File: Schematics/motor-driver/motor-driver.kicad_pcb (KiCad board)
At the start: 2 copper layers, 99.1 x 74.9 mm, 17 parts, among them J1 Conn_01x02_Male, U1 encoder-motor, U2 encoder-motor, U3 encoder-motor, U4 encoder-motor, U5 TB6612-breakout, U6 TB6612-breakout, U7 Teensy3.2

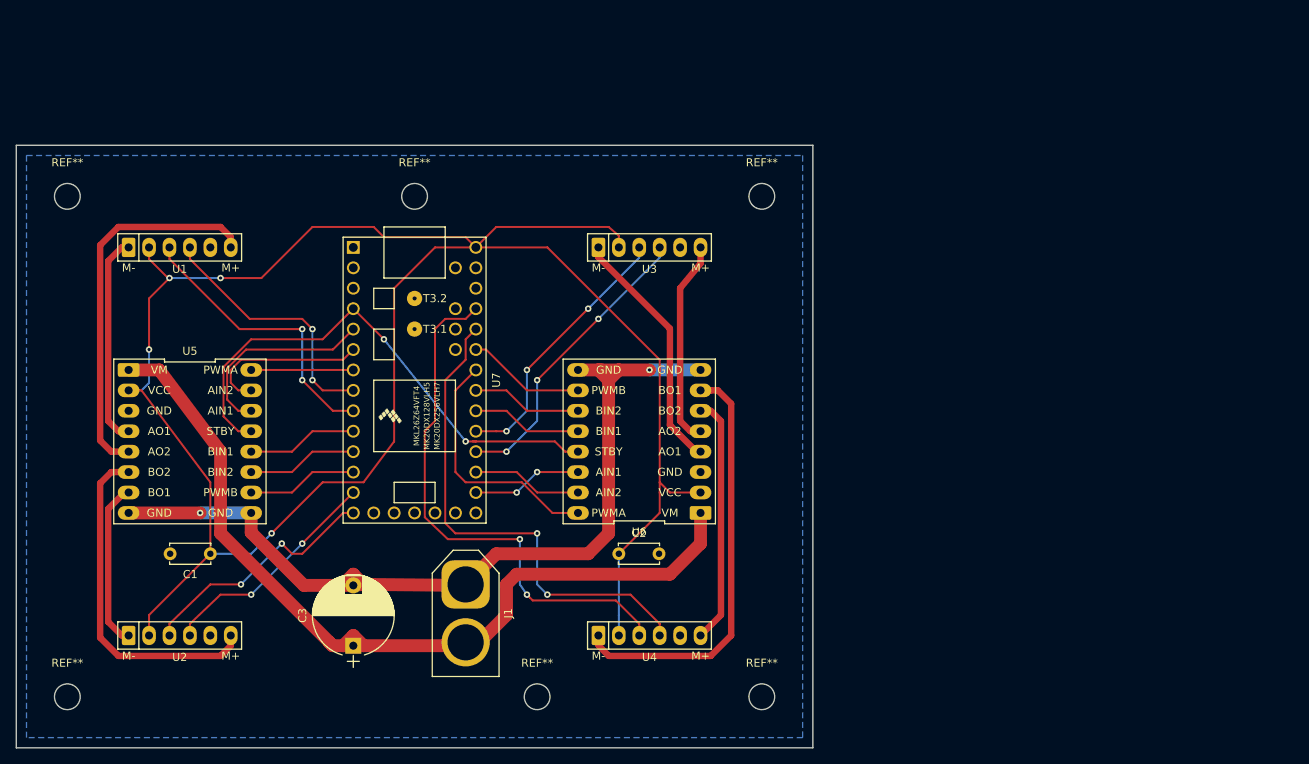
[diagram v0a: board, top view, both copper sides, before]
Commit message: Add mounting holes to PCB
Update submodule remote
Remove files that should just be wiki pages

#28, #16
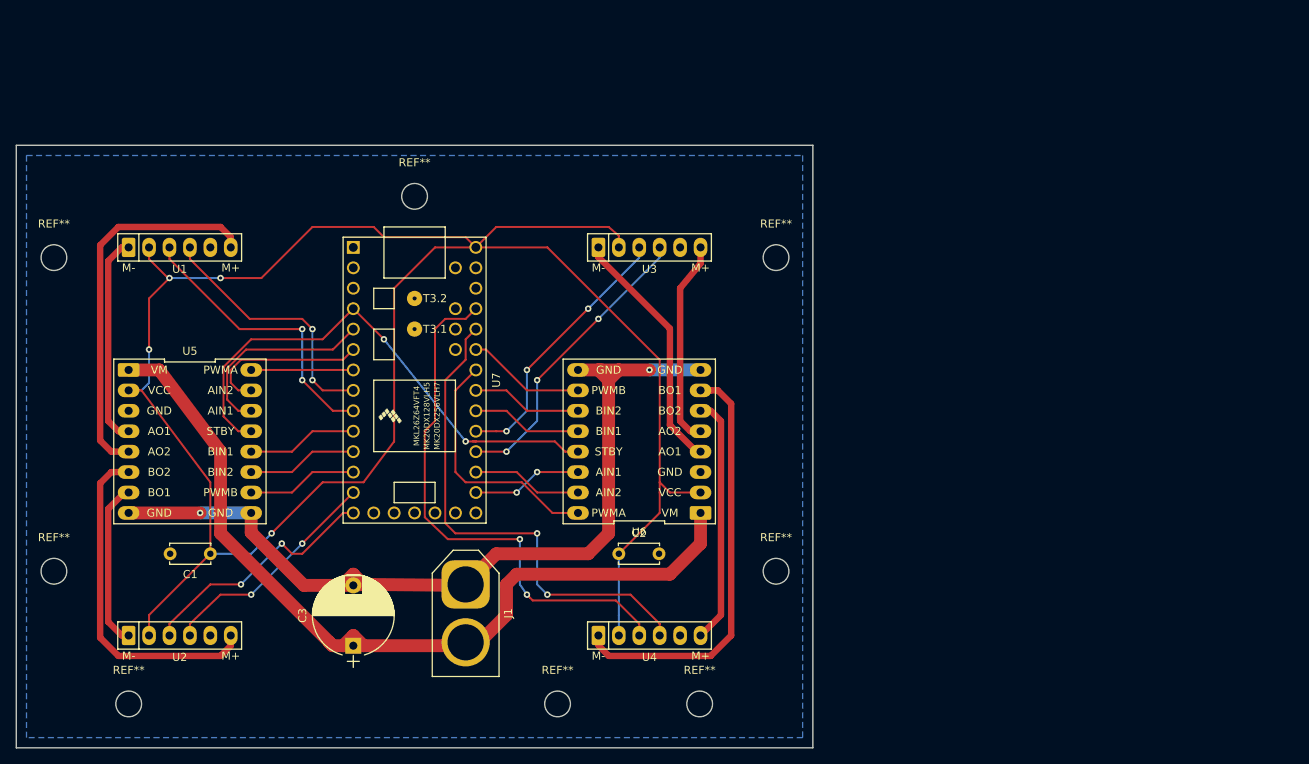
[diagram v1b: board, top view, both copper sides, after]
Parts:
- removed the REF** at (132.1, 105.4)
- removed the REF** at (45.7, 105.4)
- added REF**: MountingHole_3.2mm_M3, Mounting_Holes:MountingHole_3.2mm_M3, F.Cu at (106.7, 106.3)
- added REF**: MountingHole_3.2mm_M3, Mounting_Holes:MountingHole_3.2mm_M3, F.Cu at (53.4, 106.3)
- added REF**: MountingHole_3.2mm_M3, Mounting_Holes:MountingHole_3.2mm_M3, F.Cu at (133.8, 89.8)
- added REF**: MountingHole_3.2mm_M3, Mounting_Holes:MountingHole_3.2mm_M3, F.Cu at (44.0, 89.8)
- moved REF** 88.5 mm to (133.8, 50.8)
- moved REF** 88.4 mm to (44.0, 50.8)
- moved REF** 20.2 mm to (124.3, 106.3)
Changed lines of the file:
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@@
     (tracks 284)
     (zones 0)
-    (modules 17)
+    (modules 19)
     (nets 48)
   )
@@
       (drillshape 0)
       (scaleselection 1)
-      (outputdirectory ""))
+      (outputdirectory "plot/"))
   )
   (net 0 "")
@@
   )
   (module Mounting_Holes:MountingHole_3.2mm_M3 (layer F.Cu)
+    (at 106.68 106.3)
+    (descr "Mounting Hole 3.2mm, no annular, M3")
+    (tags "mounting hole 3.2mm no annular m3")
+    (attr virtual)
+    (fp_text reference REF** (at 0 -4.2) (layer F.SilkS)
+      (effects (font (size 1 1) (thickness 0.15)))
+    )
+    (fp_text value MountingHole_3.2mm_M3 (at 0 4.2) (layer F.Fab)
+      (effects (font (size 1 1) (thickness 0.15)))
+    )
+    (fp_circle (center 0 0) (end 3.45 0) (layer F.CrtYd) (width 0.05))
+    (fp_circle (center 0 0) (end 3.2 0) (layer Cmts.User) (width 0.15))
+    (fp_text user %R (at 0.3 0) (layer F.Fab)
+      (effects (font (size 1 1) (thickness 0.15)))
+    )
+    (pad 1 np_thru_hole circle (at 0 0) (size 3.2 3.2) (drill 3.2) (layers *.Cu *.Mask))
+  )
+  (module Mounting_Holes:MountingHole_3.2mm_M3 (layer F.Cu)
+    (at 53.35 106.3)
+    (descr "Mounting Hole 3.2mm, no annular, M3")
+    (tags "mounting hole 3.2mm no annular m3")
+    (attr virtual)
+    (fp_text reference REF** (at 0 -4.2) (layer F.SilkS)
+      (effects (font (size 1 1) (thickness 0.15)))
+    )
+    (fp_text value MountingHole_3.2mm_M3 (at 0 4.2) (layer F.Fab)
+      (effects (font (size 1 1) (thickness 0.15)))
+    )
+    (fp_circle (center 0 0) (end 3.45 0) (layer F.CrtYd) (width 0.05))
+    (fp_circle (center 0 0) (end 3.2 0) (layer Cmts.User) (width 0.15))
+    (fp_text user %R (at 0.3 0) (layer F.Fab)
+      (effects (font (size 1 1) (thickness 0.15)))
+    )
+    (pad 1 np_thru_hole circle (at 0 0) (size 3.2 3.2) (drill 3.2) (layers *.Cu *.Mask))
+  )
+  (module Mounting_Holes:MountingHole_3.2mm_M3 (layer F.Cu)
+    (at 133.85 89.8)
+    (descr "Mounting Hole 3.2mm, no annular, M3")
+    (tags "mounting hole 3.2mm no annular m3")
+    (attr virtual)
+    (fp_text reference REF** (at 0 -4.2) (layer F.SilkS)
+      (effects (font (size 1 1) (thickness 0.15)))
+    )
+    (fp_text value MountingHole_3.2mm_M3 (at 0 4.2) (layer F.Fab)
+      (effects (font (size 1 1) (thickness 0.15)))
+    )
+    (fp_circle (center 0 0) (end 3.45 0) (layer F.CrtYd) (width 0.05))
+    (fp_circle (center 0 0) (end 3.2 0) (layer Cmts.User) (width 0.15))
+    (fp_text user %R (at 0.3 0) (layer F.Fab)
+      (effects (font (size 1 1) (thickness 0.15)))
+    )
+    (pad 1 np_thru_hole circle (at 0 0) (size 3.2 3.2) (drill 3.2) (layers *.Cu *.Mask))
+  )
+  (module Mounting_Holes:MountingHole_3.2mm_M3 (layer F.Cu)
+    (at 44.05 89.8)
+    (descr "Mounting Hole 3.2mm, no annular, M3")
+    (tags "mounting hole 3.2mm no annular m3")
+    (attr virtual)
+    (fp_text reference REF** (at 0 -4.2) (layer F.SilkS)
+      (effects (font (size 1 1) (thickness 0.15)))
+    )
+    (fp_text value MountingHole_3.2mm_M3 (at 0 4.2) (layer F.Fab)
+      (effects (font (size 1 1) (thickness 0.15)))
+    )
+    (fp_circle (center 0 0) (end 3.45 0) (layer F.CrtYd) (width 0.05))
+    (fp_circle (center 0 0) (end 3.2 0) (layer Cmts.User) (width 0.15))
+    (fp_text user %R (at 0.3 0) (layer F.Fab)
+      (effects (font (size 1 1) (thickness 0.15)))
+    )
+    (pad 1 np_thru_hole circle (at 0 0) (size 3.2 3.2) (drill 3.2) (layers *.Cu *.Mask))
+  )
+  (module Mounting_Holes:MountingHole_3.2mm_M3 (layer F.Cu)
     (at 88.9 43.18)
     (descr "Mounting Hole 3.2mm, no annular, M3")
@@
   )
   (module Mounting_Holes:MountingHole_3.2mm_M3 (layer F.Cu)
-    (at 104.14 105.41)
-    (descr "Mounting Hole 3.2mm, no annular, M3")
-    (tags "mounting hole 3.2mm no annular m3")
-    (attr virtual)
-    (fp_text reference REF** (at 0 -4.2) (layer F.SilkS)
-      (effects (font (size 1 1) (thickness 0.15)))
-    )
-    (fp_text value MountingHole_3.2mm_M3 (at 0 4.2) (layer F.Fab)
-      (effects (font (size 1 1) (thickness 0.15)))
-    )
-    (fp_text user %R (at 0.3 0) (layer F.Fab)
-      (effects (font (size 1 1) (thickness 0.15)))
-    )
-    (fp_circle (center 0 0) (end 3.2 0) (layer Cmts.User) (width 0.15))
-    (fp_circle (center 0 0) (end 3.45 0) (layer F.CrtYd) (width 0.05))
-    (pad 1 np_thru_hole circle (at 0 0) (size 3.2 3.2) (drill 3.2) (layers *.Cu *.Mask))
-  )
-  (module Mounting_Holes:MountingHole_3.2mm_M3 (layer F.Cu)
-    (at 132.08 105.41)
-    (descr "Mounting Hole 3.2mm, no annular, M3")
-    (tags "mounting hole 3.2mm no annular m3")
-    (attr virtual)
-    (fp_text reference REF** (at 0 -4.2) (layer F.SilkS)
-      (effects (font (size 1 1) (thickness 0.15)))
-    )
-    (fp_text value MountingHole_3.2mm_M3 (at 0 4.2) (layer F.Fab)
-      (effects (font (size 1 1) (thickness 0.15)))
-    )
-    (fp_text user %R (at 0.3 0) (layer F.Fab)
-      (effects (font (size 1 1) (thickness 0.15)))
-    )
-    (fp_circle (center 0 0) (end 3.2 0) (layer Cmts.User) (width 0.15))
-    (fp_circle (center 0 0) (end 3.45 0) (layer F.CrtYd) (width 0.05))
-    (pad 1 np_thru_hole circle (at 0 0) (size 3.2 3.2) (drill 3.2) (layers *.Cu *.Mask))
-  )
-  (module Mounting_Holes:MountingHole_3.2mm_M3 (layer F.Cu)
-    (at 45.72 105.41)
-    (descr "Mounting Hole 3.2mm, no annular, M3")
-    (tags "mounting hole 3.2mm no annular m3")
-    (attr virtual)
-    (fp_text reference REF** (at 0 -4.2) (layer F.SilkS)
-      (effects (font (size 1 1) (thickness 0.15)))
-    )
-    (fp_text value MountingHole_3.2mm_M3 (at 0 4.2) (layer F.Fab)
-      (effects (font (size 1 1) (thickness 0.15)))
-    )
-    (fp_text user %R (at 0.3 0) (layer F.Fab)
-      (effects (font (size 1 1) (thickness 0.15)))
-    )
-    (fp_circle (center 0 0) (end 3.2 0) (layer Cmts.User) (width 0.15))
-    (fp_circle (center 0 0) (end 3.45 0) (layer F.CrtYd) (width 0.05))
-    (pad 1 np_thru_hole circle (at 0 0) (size 3.2 3.2) (drill 3.2) (layers *.Cu *.Mask))
-  )
-  (module Mounting_Holes:MountingHole_3.2mm_M3 (layer F.Cu)
-    (at 132.08 43.18)
-    (descr "Mounting Hole 3.2mm, no annular, M3")
-    (tags "mounting hole 3.2mm no annular m3")
-    (attr virtual)
-    (fp_text reference REF** (at 0 -4.2) (layer F.SilkS)
-      (effects (font (size 1 1) (thickness 0.15)))
-    )
-    (fp_text value MountingHole_3.2mm_M3 (at 0 4.2) (layer F.Fab)
-      (effects (font (size 1 1) (thickness 0.15)))
-    )
-    (fp_text user %R (at 0.3 0) (layer F.Fab)
-      (effects (font (size 1 1) (thickness 0.15)))
-    )
-    (fp_circle (center 0 0) (end 3.2 0) (layer Cmts.User) (width 0.15))
-    (fp_circle (center 0 0) (end 3.45 0) (layer F.CrtYd) (width 0.05))
-    (pad 1 np_thru_hole circle (at 0 0) (size 3.2 3.2) (drill 3.2) (layers *.Cu *.Mask))
-  )
-  (module Mounting_Holes:MountingHole_3.2mm_M3 (layer F.Cu)
-    (at 45.72 43.18)
-    (descr "Mounting Hole 3.2mm, no annular, M3")
-    (tags "mounting hole 3.2mm no annular m3")
+    (at 124.35 106.3)
+    (descr "Mounting Hole 3.2mm, no annular, M3")
+    (tags "mounting hole 3.2mm no annular m3")
+    (attr virtual)
+    (fp_text reference REF** (at 0 -4.2) (layer F.SilkS)
+      (effects (font (size 1 1) (thickness 0.15)))
+    )
+    (fp_text value MountingHole_3.2mm_M3 (at 0 4.2) (layer F.Fab)
+      (effects (font (size 1 1) (thickness 0.15)))
+    )
+    (fp_text user %R (at 0.3 0) (layer F.Fab)
+      (effects (font (size 1 1) (thickness 0.15)))
+    )
+    (fp_circle (center 0 0) (end 3.2 0) (layer Cmts.User) (width 0.15))
+    (fp_circle (center 0 0) (end 3.45 0) (layer F.CrtYd) (width 0.05))
+    (pad 1 np_thru_hole circle (at 0 0) (size 3.2 3.2) (drill 3.2) (layers *.Cu *.Mask))
+  )
+  (module Mounting_Holes:MountingHole_3.2mm_M3 (layer F.Cu)
+    (at 44.05 50.8)
+    (descr "Mounting Hole 3.2mm, no annular, M3")
+    (tags "mounting hole 3.2mm no annular m3")
+    (attr virtual)
+    (fp_text reference REF** (at 0 -4.2) (layer F.SilkS)
+      (effects (font (size 1 1) (thickness 0.15)))
+    )
+    (fp_text value MountingHole_3.2mm_M3 (at 0 4.2) (layer F.Fab)
+      (effects (font (size 1 1) (thickness 0.15)))
+    )
+    (fp_text user %R (at 0.3 0) (layer F.Fab)
+      (effects (font (size 1 1) (thickness 0.15)))
+    )
+    (fp_circle (center 0 0) (end 3.2 0) (layer Cmts.User) (width 0.15))
+    (fp_circle (center 0 0) (end 3.45 0) (layer F.CrtYd) (width 0.05))
+    (pad 1 np_thru_hole circle (at 0 0) (size 3.2 3.2) (drill 3.2) (layers *.Cu *.Mask))
+  )
+  (module Mounting_Holes:MountingHole_3.2mm_M3 (layer F.Cu)
+    (at 133.85 50.8)
+    (descr "Mounting Hole 3.2mm, no annular, M3")
+    (tags "mounting hole 3.2mm no annular m3")

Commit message: Update schematic and start on PCB layout
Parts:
- removed U6: TB6612-breakout, Rover:TB661_breakout
- removed U7: Teensy3.2, Teensy:Teensy30_31_32_LC
- added 47k1: R, Resistors_SMD:R_0805_HandSoldering, F.Cu at (120.7, 88.9)
- added C10: 0.1uF, Capacitors_SMD:C_1206_HandSoldering, F.Cu at (187.5, 41.2)
- added C4: 0.1uF, Capacitors_SMD:C_1206_HandSoldering, F.Cu at (176.2, 50.3)
- added C5: 0.1uF, Capacitors_SMD:C_1206_HandSoldering, F.Cu at (187.5, 34.9)
- added C6: 0.1uF, Capacitors_SMD:C_1206_HandSoldering, F.Cu at (176.2, 47.2)
- added C7: 0.1uF, Capacitors_SMD:C_1206_HandSoldering, F.Cu at (192.7, 30.4)
- added C8: 0.1uF, Capacitors_SMD:C_1206_HandSoldering, F.Cu at (187.5, 38.1)
- added C9: 0.1uF, Capacitors_SMD:C_1206_HandSoldering, F.Cu at (195.1, 33.5)
- added J10: I2C/Ain/PWM 5V, Rover:I2C_Ain_PWM_5V, F.Cu at (176.8, 35.7)
- added J11: PWM/PPM 5V, Rover:PPM_PWM_5V, F.Cu at (181.4, 35.7)
- added J2: SPI, Rover:SPI_3.3V, F.Cu at (76.2, 90.2)
- added J3: 32-33, Rover:32-33_3.3V, F.Cu at (182.3, 45.4)
- added J4: UART/I2C/PWM 3.3V, Rover:UART_I2C_PWM_3.3V, F.Cu at (151.1, 24.1)
- added J5: I2C/Ain/PWM 3.3V, Rover:I2C_Ain_PWM_3.3V, F.Cu at (153.7, 71.1)
- added J6: PWM/PPM 3.3V, Rover:PPM_PWM_3.3V, F.Cu at (170.1, 47.9)
- added J7: UART/Ain, Rover:UART_Ain_3.3V, F.Cu at (167.5, 35.7)
- added J8: 32-33, Rover:32-33_5V, F.Cu at (186.9, 45.1)
- added J9: UART/I2C/PWM 5V, Rover:I2C_Ain_PWM_5V, F.Cu at (172.1, 35.7)
- added M1: encoder-motor, Rover:Motor_Header_Pitch2.54mm, F.Cu at (59.7, 49.5)
- added M2: encoder-motor, Rover:Motor_Header_Pitch2.54mm, F.Cu at (59.7, 97.8)
- added M3: encoder-motor, Rover:Motor_Header_Pitch2.54mm, F.Cu at (118.1, 49.5)
- added M4: encoder-motor, Rover:Motor_Header_Pitch2.54mm, F.Cu at (118.1, 97.8)
- added R1: 47k, Resistors_SMD:R_0805_HandSoldering, F.Cu at (73.7, 54.6)
- C1, C2: value 0.1uF -> 10uF; footprint Capacitors_THT:C_Disc_D5.0mm_W2.5mm_P5.00mm -> Capacitors_SMD:C_1206_HandSoldering
- C3: value 10uF -> 0.1uF; footprint Capacitors_THT:CP_Radial_D10.0mm_P7.50mm -> Capacitors_SMD:C_1206_HandSoldering
- J1: value Conn_01x02_Male -> XT-60
- U1, U2: value encoder-motor -> TB6612FNG; footprint Rover:Motor_Header_Pitch2.54mm -> Housings_SSOP:SSOP-24_5.3x8.2mm_Pitch0.65mm
- U3, U4: value encoder-motor -> TXB0108PWR; footprint Rover:Motor_Header_Pitch2.54mm -> TXB0108PWR:TSSOP20
- U5: value TB6612-breakout -> Teensy4.0; footprint Rover:TB661_breakout -> Teensy:Teensy40
- moved U2 67.0 mm to (119.4, 67.3), turned to 180 degrees
- moved U3 45.6 mm to (73.7, 59.7), turned to 90 degrees
- moved U5 29.0 mm to (88.9, 66.0)
- moved U1 21.9 mm to (55.9, 71.1)
- moved U4 14.2 mm to (120.7, 83.8), turned to 270 degrees
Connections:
- C1 pad 1: +5V -> -BATT
- C1 pad 2: GND -> +BATT
- C2 pad 1: +5V -> -BATT
- C2 pad 2: GND -> +BATT
- C3 pad 1: +BATT -> GND
- C3 pad 2: -BATT -> +3V3
- U1 pad 2: +5V -> /M1-
- U1 pad 3: Net-(U1-Pad3) -> -BATT
- U1 pad 4: Net-(U1-Pad4) -> -BATT
- U1 pad 5: GND -> /M1+
- U2 pad 1: /M2- -> /M3-
- U2 pad 2: +5V -> /M3-
- U2 pad 3: Net-(U2-Pad3) -> -BATT
- U2 pad 4: Net-(U2-Pad4) -> -BATT
- U2 pad 5: GND -> /M3+
- U2 pad 6: /M2+ -> /M3+
- U3 pad 1: /M3- -> (no net)
- U3 pad 2: +5V -> +3V3
- U3 pad 5: GND -> Net-(U3-Pad5)
- U3 pad 6: /M3+ -> Net-(U3-Pad6)
- U4 pad 1: /M4- -> Net-(J3-Pad1)
- U4 pad 2: +5V -> +3V3
- U4 pad 3: Net-(U4-Pad3) -> Net-(J3-Pad2)
- U4 pad 5: GND -> Net-(J4-Pad1)
- U4 pad 6: /M4+ -> Net-(J4-Pad2)
- U5 pad 1: +BATT -> GND
- U5 pad 10: Net-(U5-Pad10) -> Net-(U1-Pad23)
- U5 pad 11: Net-(U5-Pad11) -> Net-(U1-Pad15)
- U5 pad 13: STBY -> Net-(J2-Pad5)
- U5 pad 15: Net-(U5-Pad15) -> (no net)
- U5 pad 16: Net-(U5-Pad16) -> (no net)
- U5 pad 2: +5V -> Net-(U3-Pad9)
- U5 pad 3: GND -> Net-(U3-Pad8)
- U5 pad 4: /M1- -> Net-(U3-Pad7)
- U5 pad 5: /M1+ -> Net-(U3-Pad6)
- U5 pad 6: /M2+ -> Net-(U3-Pad5)
- U5 pad 7: /M2- -> Net-(U3-Pad4)
- U5 pad 8: -BATT -> Net-(J6-Pad3)
- U5 pad 9: -BATT -> Net-(U3-Pad3)
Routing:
- net +5V: track 253.6 -> 0.00 mm, vias 4 -> 0
- net -BATT: track 109.2 -> 0.00 mm, vias 3 -> 0
- net +BATT: track 107.1 -> 0.00 mm
- net Net-(U4-Pad3): track 67.1 -> 0.00 mm, vias 2 -> 0
- net STBY: track 66.0 -> 0.00 mm, vias 2 -> 0
- net Net-(U4-Pad4): track 62.7 -> 0.00 mm, vias 2 -> 0
- net /M4-: track 53.9 -> 0.00 mm
- net /M1+: track 47.4 -> 0.00 mm
- net /M2+: track 42.3 -> 0.00 mm
- net Net-(U3-Pad4): track 37.1 -> 0.00 mm, vias 3 -> 0
- net Net-(U1-Pad3): track 35.8 -> 0.00 mm, vias 2 -> 0
- net Net-(U3-Pad3): track 33.5 -> 0.00 mm, vias 4 -> 0
- net Net-(U1-Pad4): track 32.3 -> 0.00 mm, vias 2 -> 0
- net /M3-: track 32.2 -> 0.00 mm
- net /M4+: track 31.3 -> 0.00 mm
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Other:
- net class VCC added: clearance 0.2, trace_width 0.35, via_dia 0.8, via_drill 0.4
